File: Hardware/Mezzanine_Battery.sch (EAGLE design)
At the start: 8 parts, among them U2 EDISON_CONNECTOR_FULLMOUNTING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, U3 EDISON_CONNECTOR_FULLHEADER

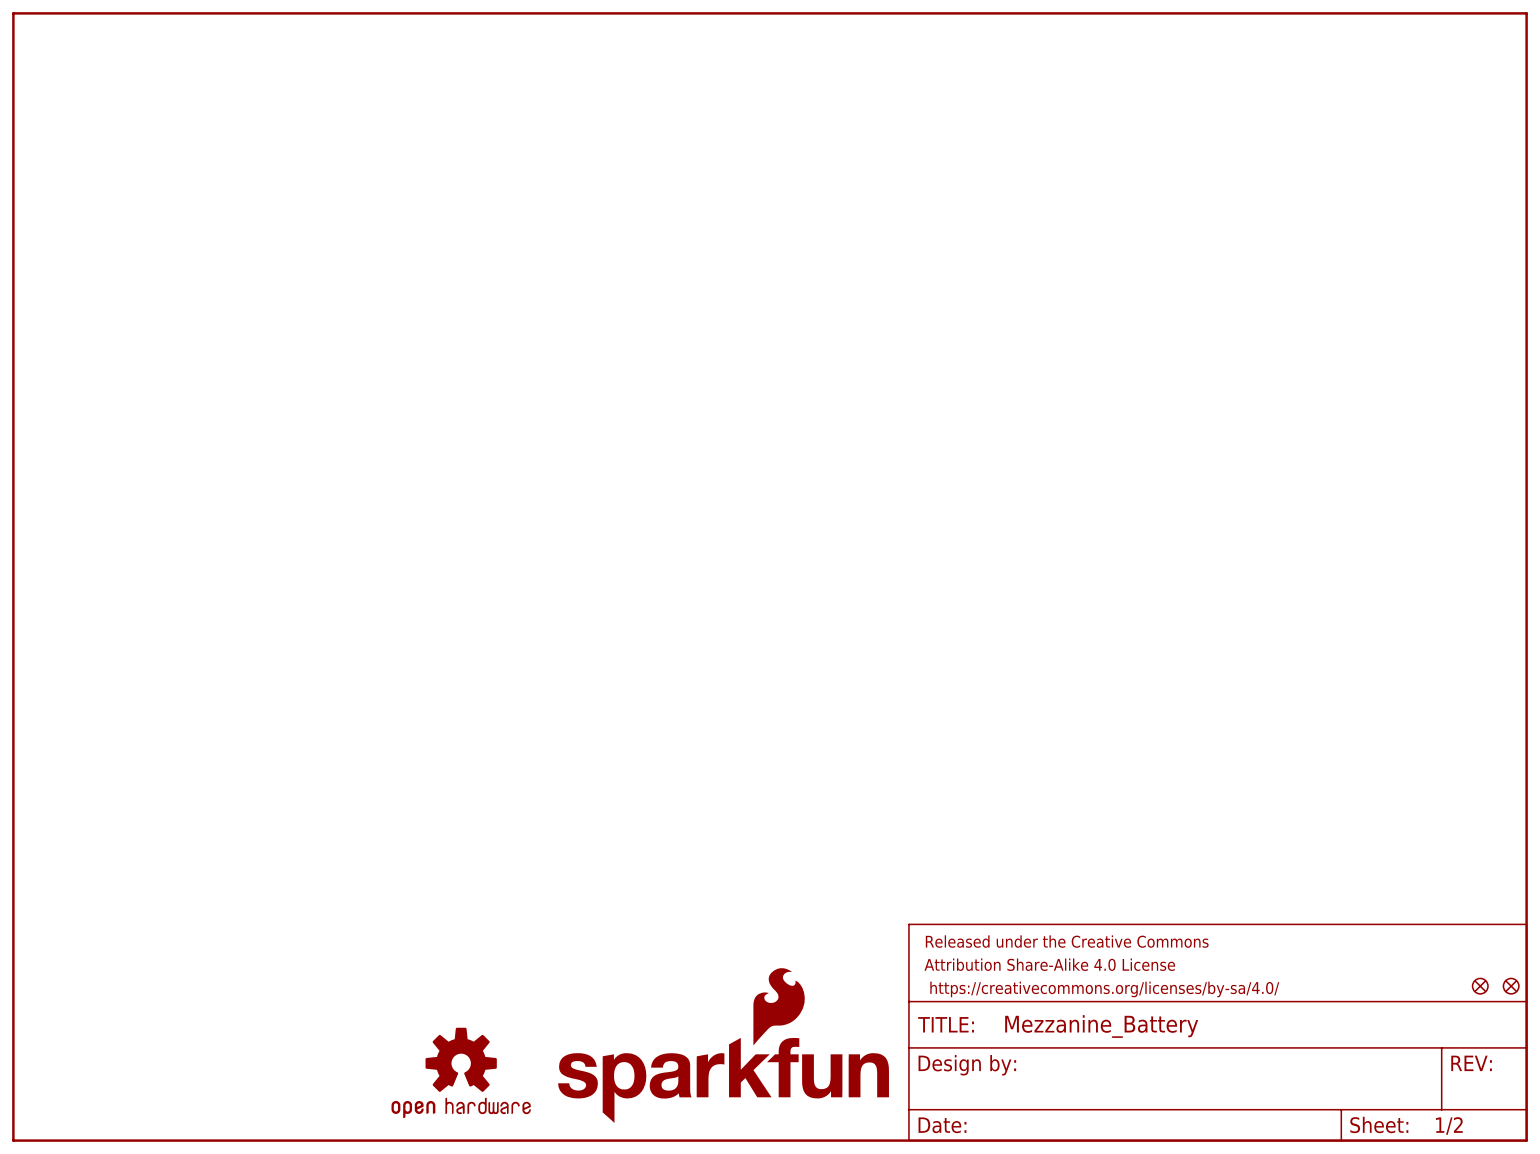
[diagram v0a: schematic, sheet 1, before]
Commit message: layout ready for review. Renamed boards
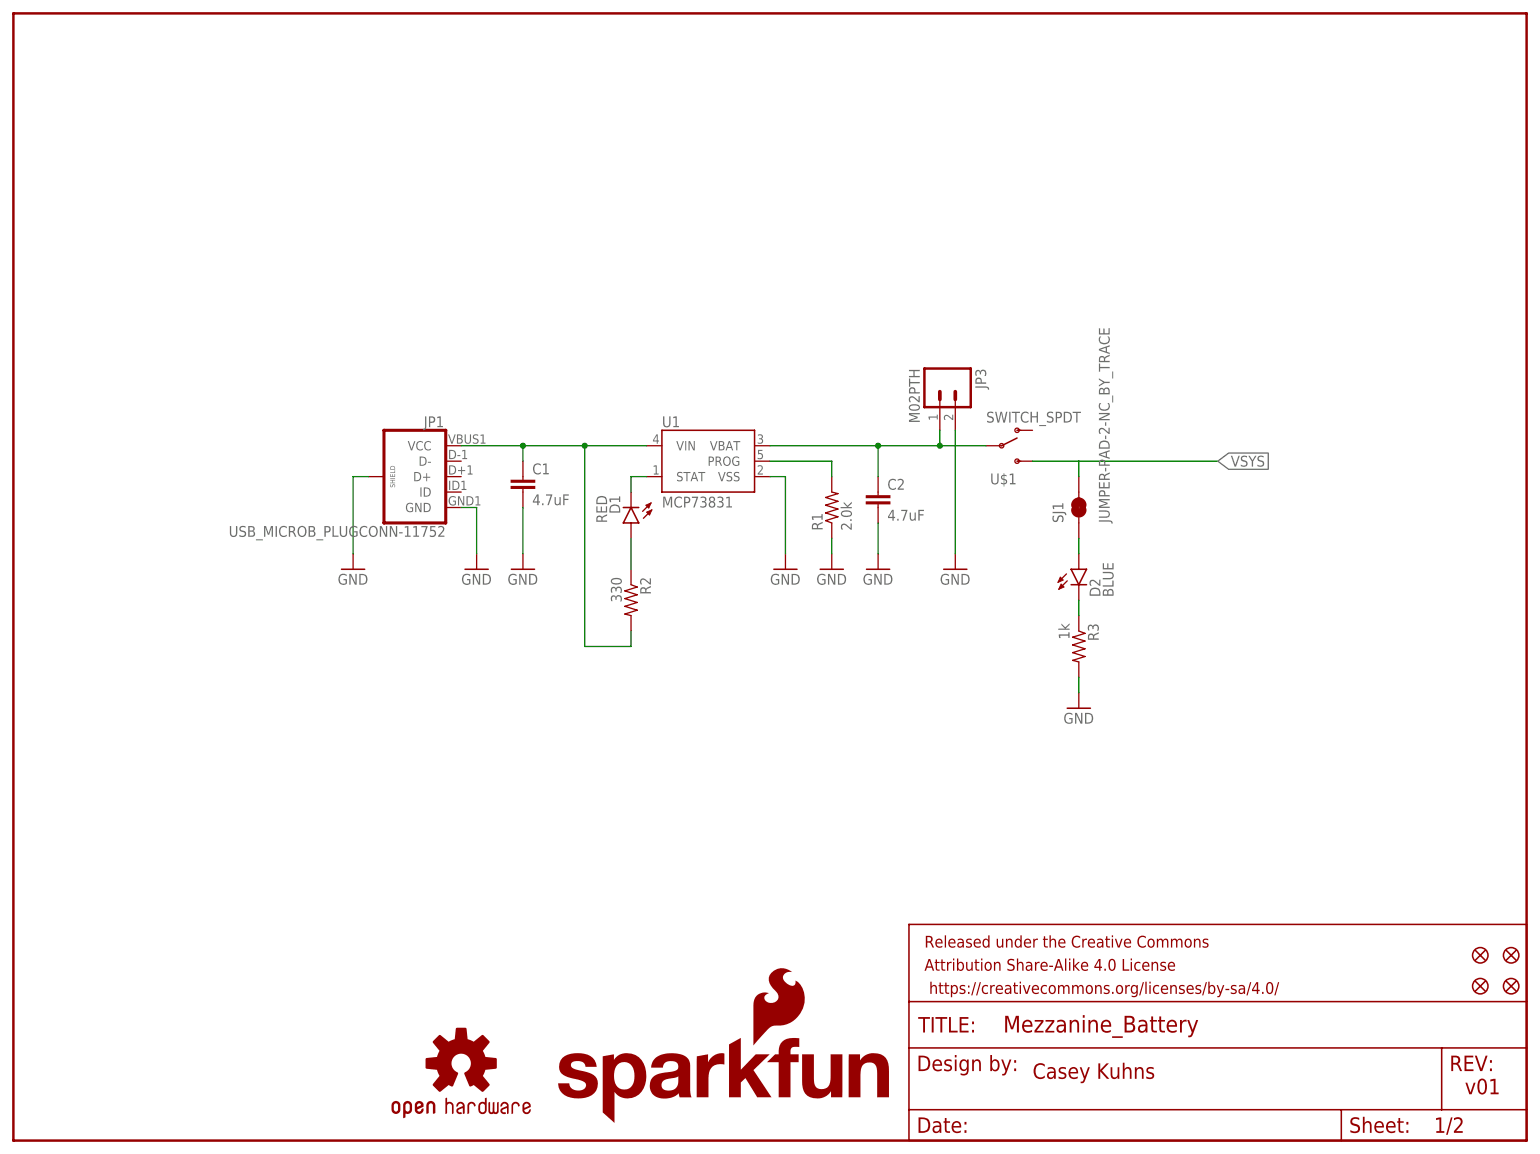
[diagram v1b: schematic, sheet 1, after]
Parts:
- added C1, C2: 4.7uF, SparkFun-Capacitors:4.7UF-6.3V-10%(0603)0603
- added D1: RED, SparkFun-LED:LED-RED0603
- added D2: BLUE, SparkFun-LED:LED-BLUE0603
- added FID3, FID4: FIDUCIAL1X2, SparkFun-Aesthetics:FIDUCIAL1X2
- added JP1: USB_MICROB_PLUGCONN-11752, SparkFun-Connectors:USB_MICROB_PLUGCONN-11752
- added JP3: M02PTH, SparkFun-Connectors:M02PTH
- added R1: 2.0k, SparkFun-Resistors:2.0KOHM1/10W5%(0603)
- added R2: 330, SparkFun-Resistors:330OHM1/10W1%(0603)
- added R3: 1k, SparkFun-Resistors:1KOHM1/10W1%(0603)
- added SJ1: JUMPER-PAD-2-NC_BY_TRACE, SparkFun-Passives:JUMPER-PAD-2-NC_BY_TRACE
- added U$1: SWITCH_SPDT, SparkFun-Electromechanical:SWITCH_SPDT
- added U1: MCP73831, SparkFun-PowerIC:MCP73831
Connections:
- new net N$1: C1.1, JP1.VCC, R2.2, U1.VIN
- new net N$2: D2.C, R3.1
- new net N$3: R1.2, U1.PROG
- new net N$4: D1.A, R2.1
- new net N$5: D1.C, U1.STAT
- new net N$6: C2.1, JP3.1, U$1.P, U1.VBAT
- new net N$7: D2.A, SJ1.1
- net GND: now also C1.2, C2.2, JP1.GND, JP1.SHIELD, JP3.2, R1.1, R3.2, U1.VSS
- net VSYS: now also SJ1.2, U$1.S
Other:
- note added: "Casey Kuhns"
- note added: "v01"
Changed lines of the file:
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@@
 <part name="FID1" library="SparkFun-Aesthetics" deviceset="FIDUCIAL" device="1X2"/>
 <part name="FID2" library="SparkFun-Aesthetics" deviceset="FIDUCIAL" device="1X2"/>
+<part name="JP1" library="SparkFun-Connectors" deviceset="USB_MICROB_PLUG" device="CONN-11752"/>
+<part name="GND1" library="SparkFun-Aesthetics" deviceset="GND" device=""/>
+<part name="GND2" library="SparkFun-Aesthetics" deviceset="GND" device=""/>
+<part name="C1" library="SparkFun-Capacitors" deviceset="4.7UF-6.3V-10%(0603)" device="0603" value="4.7uF"/>
+<part name="U$1" library="SparkFun-Electromechanical" deviceset="SWITCH_SPDT" device=""/>
+<part name="R1" library="SparkFun-Resistors" deviceset="2.0KOHM1/10W5%(0603)" device="" value="2.0k"/>
+<part name="JP3" library="SparkFun-Connectors" deviceset="M02" device="PTH"/>
+<part name="R2" library="SparkFun-Resistors" deviceset="330OHM1/10W1%(0603)" device="" value="330"/>
+<part name="U1" library="SparkFun-PowerIC" deviceset="MCP73831" device=""/>
+<part name="GND5" library="SparkFun-Aesthetics" deviceset="GND" device=""/>
+<part name="GND6" library="SparkFun-Aesthetics" deviceset="GND" device=""/>
+<part name="GND7" library="SparkFun-Aesthetics" deviceset="GND" device=""/>
+<part name="D1" library="SparkFun-LED" deviceset="LED-RED" device="0603" value="RED"/>
+<part name="C2" library="SparkFun-Capacitors" deviceset="4.7UF-6.3V-10%(0603)" device="0603" value="4.7uF"/>
+<part name="GND8" library="SparkFun-Aesthetics" deviceset="GND" device=""/>
+<part name="GND10" library="SparkFun-Aesthetics" deviceset="GND" device=""/>
+<part name="D2" library="SparkFun-LED" deviceset="LED-BLUE" device="0603" value="BLUE"/>
+<part name="R3" library="SparkFun-Resistors" deviceset="1KOHM1/10W1%(0603)" device="" value="1k"/>
+<part name="GND9" library="SparkFun-Aesthetics" deviceset="GND" device=""/>
+<part name="SJ1" library="SparkFun-Passives" deviceset="JUMPER-PAD-2-NC_BY_TRACE" device=""/>
+<part name="FID3" library="SparkFun-Aesthetics" deviceset="FIDUCIAL" device="1X2"/>
+<part name="FID4" library="SparkFun-Aesthetics" deviceset="FIDUCIAL" device="1X2"/>
 </parts>
 <sheets>
 <sheet>
 <plain>
+<text x="167.64" y="10.16" size="2.54" layer="94">Casey Kuhns</text>
+<text x="238.76" y="7.62" size="2.54" layer="94">v01</text>
 </plain>
 <instances>
@@
 <instance part="FID1" gate="G$1" x="246.38" y="25.4"/>
 <instance part="FID2" gate="G$1" x="241.3" y="25.4"/>
+<instance part="JP1" gate="G$1" x="66.04" y="109.22" rot="MR0"/>
+<instance part="GND1" gate="1" x="76.2" y="93.98"/>
+<instance part="GND2" gate="1" x="55.88" y="93.98"/>
+<instance part="C1" gate="G$1" x="83.82" y="106.68"/>
+<instance part="U$1" gate="G$1" x="162.56" y="114.3"/>
+<instance part="R1" gate="G$1" x="134.62" y="104.14" rot="R90"/>
+<instance part="JP3" gate="G$1" x="152.4" y="124.46" rot="R270"/>
+<instance part="R2" gate="G$1" x="101.6" y="88.9" rot="R270"/>
+<instance part="U1" gate="G$1" x="114.3" y="111.76"/>
+<instance part="GND5" gate="1" x="83.82" y="93.98"/>
+<instance part="GND6" gate="1" x="127" y="93.98"/>
+<instance part="GND7" gate="1" x="134.62" y="93.98"/>
+<instance part="D1" gate="G$1" x="101.6" y="101.6" rot="R180"/>
+<instance part="C2" gate="G$1" x="142.24" y="104.14"/>
+<instance part="GND8" gate="1" x="142.24" y="93.98"/>
+<instance part="GND10" gate="1" x="154.94" y="93.98"/>
+<instance part="D2" gate="G$1" x="175.26" y="93.98"/>
+<instance part="R3" gate="G$1" x="175.26" y="81.28" rot="R270"/>
+<instance part="GND9" gate="1" x="175.26" y="71.12"/>
+<instance part="SJ1" gate="G$1" x="175.26" y="104.14" rot="R90"/>
+<instance part="FID3" gate="G$1" x="246.38" y="30.48"/>
+<instance part="FID4" gate="G$1" x="241.3" y="30.48"/>
 </instances>
 <busses>
 </busses>
 <nets>
+<net name="GND" class="0">
+<segment>
+<pinref part="GND2" gate="1" pin="GND"/>
+<pinref part="JP1" gate="G$1" pin="SHIELD"/>
+<wire x1="55.88" y1="96.52" x2="55.88" y2="109.22" width="0.1524" layer="91"/>
+<wire x1="55.88" y1="109.22" x2="58.42" y2="109.22" width="0.1524" layer="91"/>
+</segment>
+<segment>
+<pinref part="JP1" gate="G$1" pin="GND"/>
+<pinref part="GND1" gate="1" pin="GND"/>
+<wire x1="73.66" y1="104.14" x2="76.2" y2="104.14" width="0.1524" layer="91"/>
+<wire x1="76.2" y1="104.14" x2="76.2" y2="96.52" width="0.1524" layer="91"/>
+</segment>
+<segment>
+<pinref part="U1" gate="G$1" pin="VSS"/>
+<wire x1="124.46" y1="109.22" x2="127" y2="109.22" width="0.1524" layer="91"/>
+<wire x1="127" y1="109.22" x2="127" y2="96.52" width="0.1524" layer="91"/>
+<pinref part="GND6" gate="1" pin="GND"/>
+</segment>
+<segment>
+<pinref part="C1" gate="G$1" pin="2"/>
+<pinref part="GND5" gate="1" pin="GND"/>
+<wire x1="83.82" y1="104.14" x2="83.82" y2="96.52" width="0.1524" layer="91"/>
+</segment>
+<segment>
+<pinref part="R1" gate="G$1" pin="1"/>
+<pinref part="GND7" gate="1" pin="GND"/>
+<wire x1="134.62" y1="99.06" x2="134.62" y2="96.52" width="0.1524" layer="91"/>
+</segment>
+<segment>
+<pinref part="C2" gate="G$1" pin="2"/>
+<wire x1="142.24" y1="101.6" x2="142.24" y2="96.52" width="0.1524" layer="91"/>
+<pinref part="GND8" gate="1" pin="GND"/>
+</segment>
+<segment>
+<pinref part="JP3" gate="G$1" pin="2"/>
+<wire x1="154.94" y1="116.84" x2="154.94" y2="96.52" width="0.1524" layer="91"/>
+<pinref part="GND10" gate="1" pin="GND"/>
+</segment>
+<segment>
+<pinref part="R3" gate="G$1" pin="2"/>
+<pinref part="GND9" gate="1" pin="GND"/>
+<wire x1="175.26" y1="73.66" x2="175.26" y2="76.2" width="0.1524" layer="91"/>
+</segment>
+</net>
+<net name="N$1" class="0">
+<segment>
+<pinref part="JP1" gate="G$1" pin="VCC"/>
+<pinref part="U1" gate="G$1" pin="VIN"/>
+<wire x1="73.66" y1="114.3" x2="83.82" y2="114.3" width="0.1524" layer="91"/>
+<pinref part="C1" gate="G$1" pin="1"/>
+<wire x1="83.82" y1="114.3" x2="93.98" y2="114.3" width="0.1524" layer="91"/>
+<wire x1="93.98" y1="114.3" x2="104.14" y2="114.3" width="0.1524" layer="91"/>
+<wire x1="83.82" y1="111.76" x2="83.82" y2="114.3" width="0.1524" layer="91"/>
+<wire x1="93.98" y1="114.3" x2="93.98" y2="81.28" width="0.1524" layer="91"/>
+<wire x1="93.98" y1="81.28" x2="101.6" y2="81.28" width="0.1524" layer="91"/>
+<pinref part="R2" gate="G$1" pin="2"/>
+<wire x1="101.6" y1="81.28" x2="101.6" y2="83.82" width="0.1524" layer="91"/>
+<junction x="83.82" y="114.3"/>
+<junction x="93.98" y="114.3"/>
+</segment>
+</net>
+<net name="N$3" class="0">
+<segment>
+<pinref part="U1" gate="G$1" pin="PROG"/>
+<pinref part="R1" gate="G$1" pin="2"/>
+<wire x1="124.46" y1="111.76" x2="134.62" y2="111.76" width="0.1524" layer="91"/>
+<wire x1="134.62" y1="111.76" x2="134.62" y2="109.22" width="0.1524" layer="91"/>
+</segment>
+</net>
+<net name="N$4" class="0">
+<segment>
+<pinref part="R2" gate="G$1" pin="1"/>
+<pinref part="D1" gate="G$1" pin="A"/>
+<wire x1="101.6" y1="93.98" x2="101.6" y2="99.06" width="0.1524" layer="91"/>
+</segment>
+</net>
+<net name="N$5" class="0">
+<segment>
+<pinref part="U1" gate="G$1" pin="STAT"/>
+<pinref part="D1" gate="G$1" pin="C"/>
+<wire x1="104.14" y1="109.22" x2="101.6" y2="109.22" width="0.1524" layer="91"/>
+<wire x1="101.6" y1="109.22" x2="101.6" y2="106.68" width="0.1524" layer="91"/>
+</segment>
+</net>
+<net name="N$6" class="0">
+<segment>
+<pinref part="U1" gate="G$1" pin="VBAT"/>
+<pinref part="C2" gate="G$1" pin="1"/>
+<wire x1="124.46" y1="114.3" x2="142.24" y2="114.3" width="0.1524" layer="91"/>
+<wire x1="142.24" y1="114.3" x2="142.24" y2="109.22" width="0.1524" layer="91"/>
+<pinref part="JP3" gate="G$1" pin="1"/>
+<wire x1="142.24" y1="114.3" x2="152.4" y2="114.3" width="0.1524" layer="91"/>
+<wire x1="152.4" y1="114.3" x2="152.4" y2="116.84" width="0.1524" layer="91"/>
+<junction x="142.24" y="114.3"/>
+<pinref part="U$1" gate="G$1" pin="P"/>
+<wire x1="152.4" y1="114.3" x2="160.02" y2="114.3" width="0.1524" layer="91"/>
+<junction x="152.4" y="114.3"/>
+</segment>
+</net>
+<net name="VSYS" class="0">
+<segment>
+<pinref part="U$1" gate="G$1" pin="S"/>
+<wire x1="167.64" y1="111.76" x2="175.26" y2="111.76" width="0.1524" layer="91"/>
+<label x="198.12" y="111.76" size="1.778" layer="95" xref="yes"/>
+<pinref part="SJ1" gate="G$1" pin="2"/>
+<wire x1="175.26" y1="111.76" x2="198.12" y2="111.76" width="0.1524" layer="91"/>
+<wire x1="175.26" y1="109.22" x2="175.26" y2="111.76" width="0.1524" layer="91"/>
+</segment>
+</net>
+<net name="N$2" class="0">
+<segment>
+<pinref part="D2" gate="G$1" pin="C"/>
+<pinref part="R3" gate="G$1" pin="1"/>
+<wire x1="175.26" y1="86.36" x2="175.26" y2="88.9" width="0.1524" layer="91"/>
+</segment>
+</net>
+<net name="N$7" class="0">
+<segment>
+<pinref part="D2" gate="G$1" pin="A"/>
+<pinref part="SJ1" gate="G$1" pin="1"/>
+<wire x1="175.26" y1="96.52" x2="175.26" y2="99.06" width="0.1524" layer="91"/>
+</segment>
+</net>
 </nets>
 </sheet>
